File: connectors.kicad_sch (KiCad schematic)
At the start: 15 parts, among them J1 Compute-Module-4_Plug_Connect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, Q3 DZDH0401DW, Q9 AO3401A, U20 NTS0102_XSON, U21 NTS0102_XSON

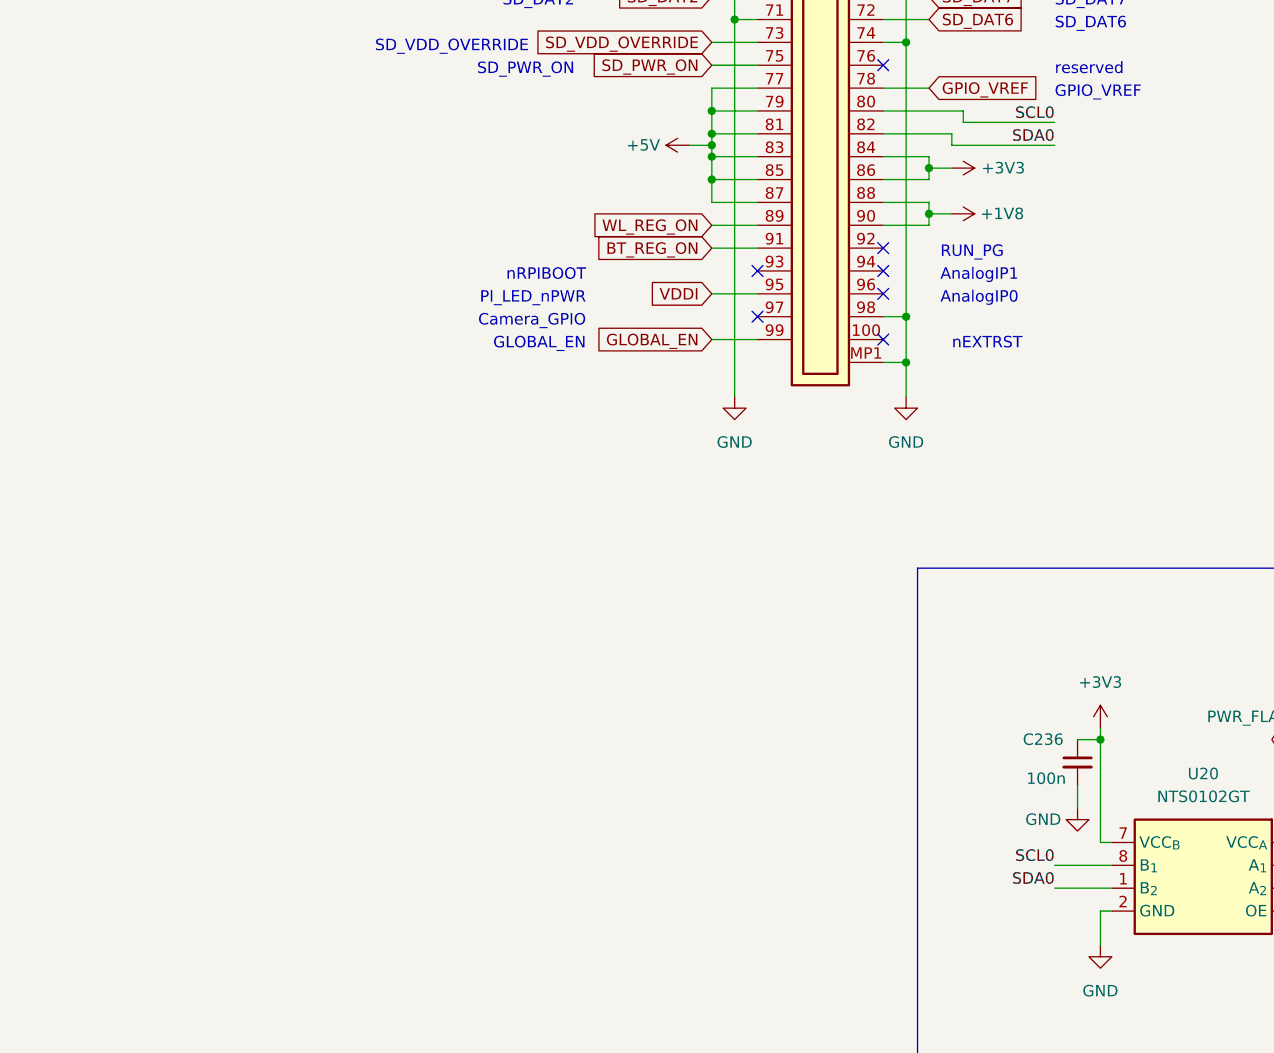
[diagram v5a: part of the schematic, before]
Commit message: [#57422] Update PI_LED_nPWR pin connection
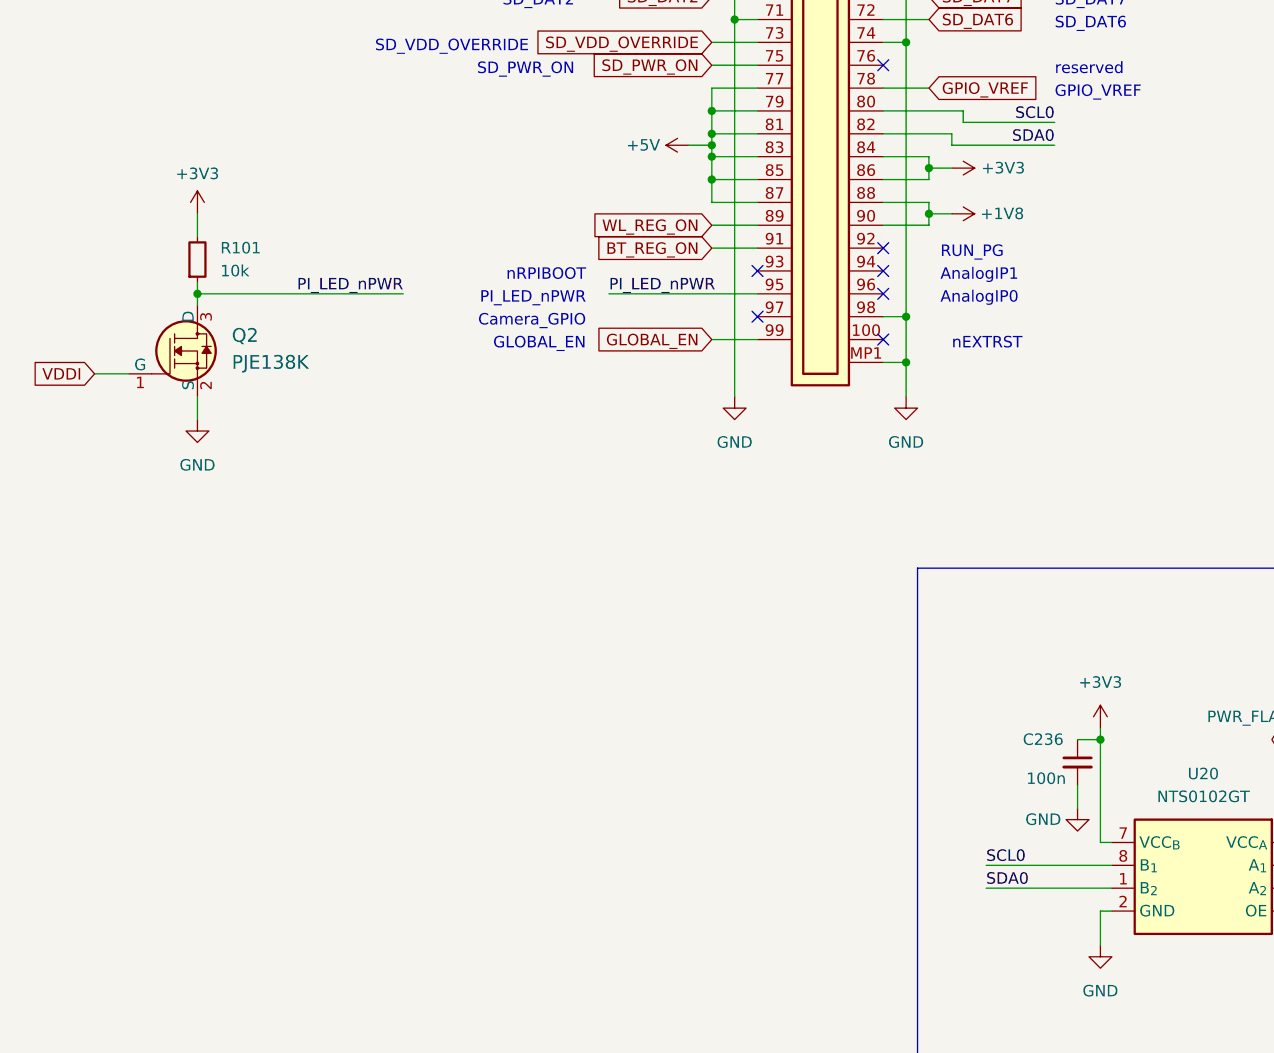
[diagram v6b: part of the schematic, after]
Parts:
- added Q2: PJE138K, antmicro-footprints:SOT-523, symbol antmicroTransistorsFETsMOSFETsSingle:PJE138K
- added R101: R_10k_0402, antmicro-footprints:R_0402_1005Metric, symbol antmicroResistors0402:R_10k_0402
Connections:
- net +3V3: now also R101.2
- net GND: now also Q2.2 (S)
- net VDDI: now also Q2.1 (G); no longer J1.95
- new net PI_LED_nPWR: J1.95, Q2.3 (D), R101.1

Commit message: [#57422] Update DNP
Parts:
- R15, R62: now not fitted
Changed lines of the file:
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@@
   )
   (symbol (lib_id "antmicroResistors0402:R_10k_0402") (at 170.18 140.97 180) (unit 1)
-    (in_bom yes) (on_board yes) (dnp no)
+    (in_bom yes) (on_board yes) (dnp yes)
     (property "Reference" "R15" (at 161.29 142.24 0)
       (effects (font (size 1.27 1.27) (thickness 0.15)) (justify right))
@@
     )
     (property "DNP" "DNP" (at 167.64 140.97 0)
-      (effects (font (size 1.27 1.27)))
+      (effects (font (size 1.27 1.27)) hide)
     )
     (pin "1")
@@
   )
   (symbol (lib_id "antmicroResistors0603:R_0R_22.4A_0603") (at 227.33 124.46 0) (unit 1)
-    (in_bom yes) (on_board yes) (dnp no)
+    (in_bom yes) (on_board yes) (dnp yes)
     (property "Reference" "R62" (at 229.87 119.38 0)
       (effects (font (size 1.27 1.27) (thickness 0.15)))
@@
     )
     (property "DNP" "DNP" (at 229.87 124.46 0)
-      (effects (font (size 1.27 1.27)))
+      (effects (font (size 1.27 1.27)) hide)
     )
     (pin "1")

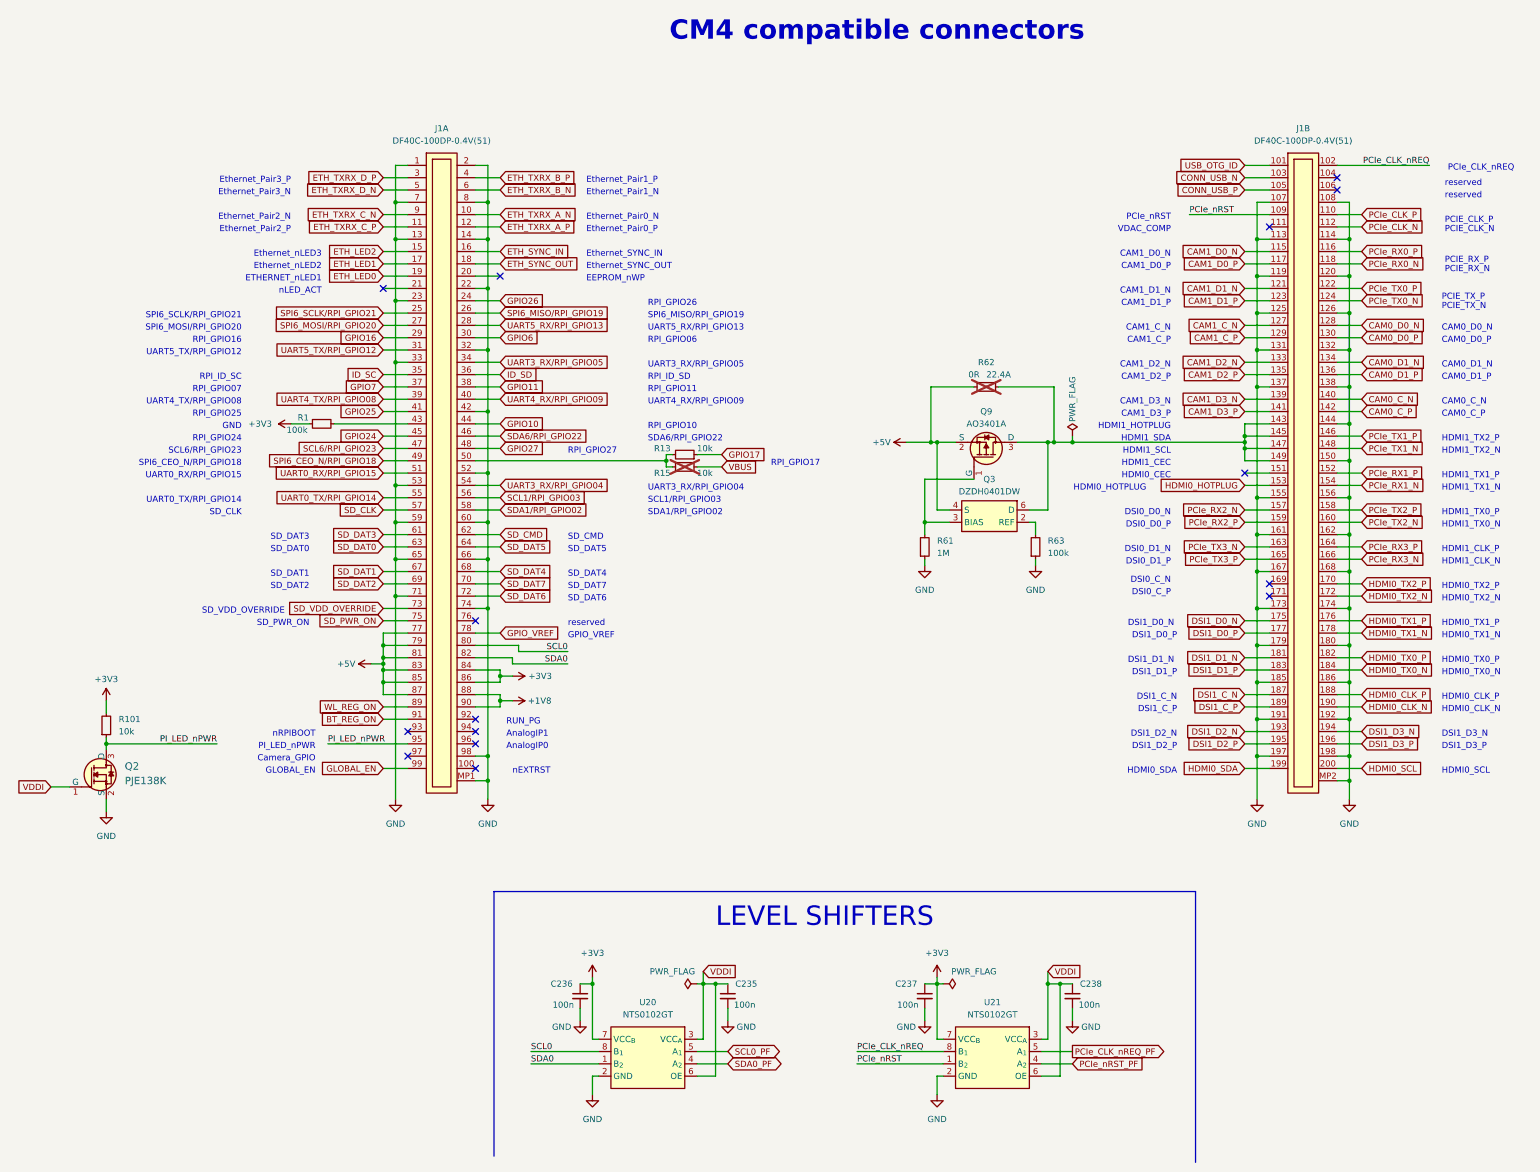
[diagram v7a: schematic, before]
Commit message: [#57505] Start reworking schematic to hierarchical structure
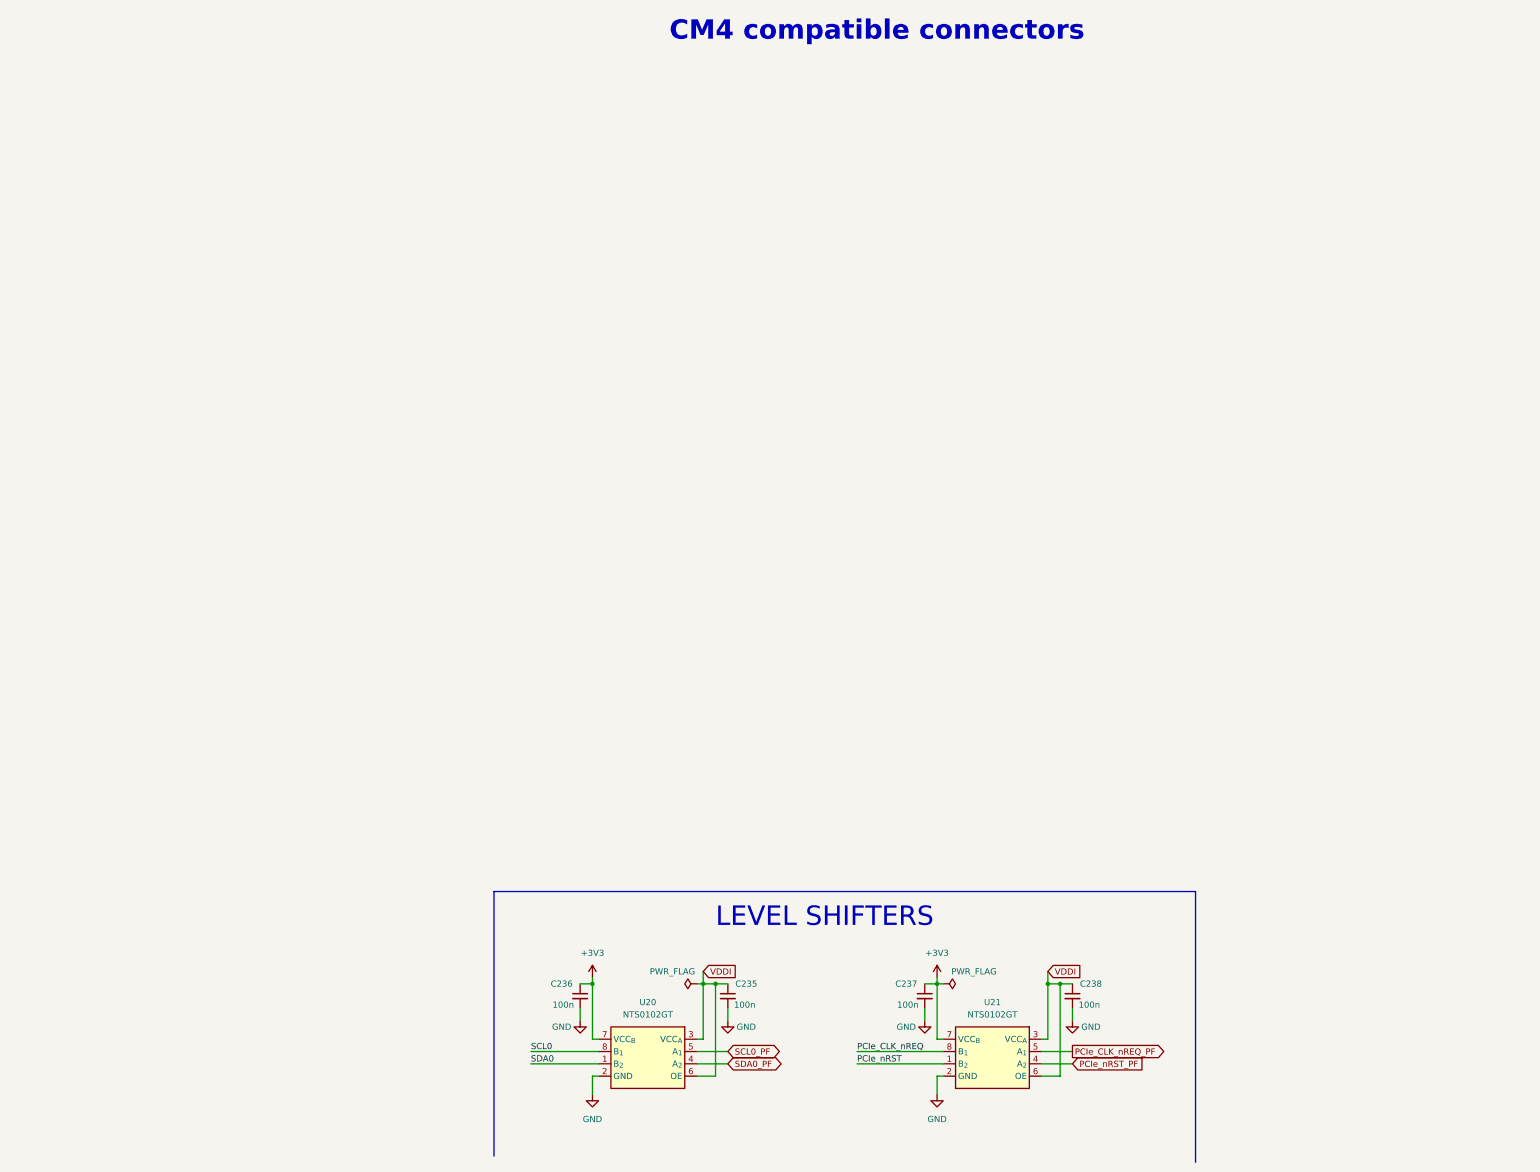
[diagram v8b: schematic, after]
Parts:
- removed J1: Compute-Module-4_Plug_Connector, antmicro-footprints:Compute-Module-4_Plug_Connector, symbol antmicroModules:Compute-Module-4_Plug_Connector
- removed Q2: PJE138K, antmicro-footprints:SOT-523, symbol antmicroTransistorsFETsMOSFETsSingle:PJE138K
- removed Q3: DZDH0401DW, antmicro-footprints:SOT-363, symbol antmicroPMICORControllersIdealDiodes:DZDH0401DW
- removed Q9: AO3401A, antmicro-footprints:SOT-23-3, symbol antmicroTransistorsFETsMOSFETsSingle:AO3401A
- removed R1, R63: R_100k_0402, antmicro-footprints:R_0402_1005Metric, symbol antmicroResistors0402:R_100k_0402
- removed R101, R13, R15: R_10k_0402, antmicro-footprints:R_0402_1005Metric, symbol antmicroResistors0402:R_10k_0402
- removed R61: R_1M_0402, antmicro-footprints:R_0402_1005Metric, symbol antmicroResistors0402:R_1M_0402
- removed R62: R_0R_22.4A_0603, antmicro-footprints:R_0603_1608Metric, symbol antmicroResistors0603:R_0R_22.4A_0603
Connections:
- no-connect marks 15 -> 0
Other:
- note removed: "AnalogIP0"
- note removed: "AnalogIP1"
- note removed: "CAM0_C_N"
- note removed: "CAM0_C_P"
- note removed: "CAM0_D0_N"
- note removed: "CAM0_D0_P"
- note removed: "CAM0_D1_N"
- note removed: "CAM0_D1_P"
- note removed: "CAM1_C_N"
- note removed: "CAM1_C_P"
- note removed: "CAM1_D0_N"
- note removed: "CAM1_D0_P"
- note removed: "CAM1_D1_N"
- note removed: "CAM1_D1_P"
- note removed: "CAM1_D2_N"
- note removed: "CAM1_D2_P"
- note removed: "CAM1_D3_N"
- note removed: "CAM1_D3_P"
- note removed: "Camera_GPIO"
- note removed: "DSI0_C_N"
- note removed: "DSI0_C_P"
- note removed: "DSI0_D0_N"
- note removed: "DSI0_D0_P"
- note removed: "DSI0_D1_N"
- note removed: "DSI0_D1_P"
- note removed: "DSI1_C_N"
- note removed: "DSI1_C_P"
- note removed: "DSI1_D0_N"
- note removed: "DSI1_D0_P"
- note removed: "DSI1_D1_N"
- note removed: "DSI1_D1_P"
- note removed: "DSI1_D2_N"
- note removed: "DSI1_D2_P"
- note removed: "DSI1_D3_N"
- note removed: "DSI1_D3_P"
- note removed: "EEPROM_nWP"
- note removed: "ETHERNET_nLED1"
- note removed: "Ethernet_Pair0_N"
- note removed: "Ethernet_Pair0_P"
- note removed: "Ethernet_Pair1_N"
- note removed: "Ethernet_Pair1_P"
- note removed: "Ethernet_Pair2_N"
- note removed: "Ethernet_Pair2_P"
- note removed: "Ethernet_Pair3_N"
- note removed: "Ethernet_Pair3_P"
- note removed: "Ethernet_SYNC_IN"
- note removed: "Ethernet_SYNC_OUT"
- note removed: "Ethernet_nLED2"
- note removed: "Ethernet_nLED3"
- note removed: "GLOBAL_EN"
- note removed: "GND"
- note removed: "GPIO_VREF"
- note removed: "HDMI0_CEC"
- note removed: "HDMI0_CLK_N"
- note removed: "HDMI0_CLK_P"
- note removed: "HDMI0_HOTPLUG"
- note removed: "HDMI0_SCL"
- note removed: "HDMI0_SDA"
- note removed: "HDMI0_TX0_N"
- note removed: "HDMI0_TX0_P"
- note removed: "HDMI0_TX1_N"
- note removed: "HDMI0_TX1_P"
- note removed: "HDMI0_TX2_N"
- note removed: "HDMI0_TX2_P"
- note removed: "HDMI1_CEC"
- note removed: "HDMI1_CLK_N"
- note removed: "HDMI1_CLK_P"
- note removed: "HDMI1_HOTPLUG"
- note removed: "HDMI1_SCL"
- note removed: "HDMI1_SDA"
- note removed: "HDMI1_TX0_N"
- note removed: "HDMI1_TX0_P"
- note removed: "HDMI1_TX1_N"
- note removed: "HDMI1_TX1_P"
- note removed: "HDMI1_TX2_N"
- note removed: "HDMI1_TX2_P"
- note removed: "PCIE_CLK_N"
- note removed: "PCIE_CLK_P"
- note removed: "PCIE_RX_N"
- note removed: "PCIE_RX_P"
- note removed: "PCIE_TX_N"
- note removed: "PCIE_TX_P"
- note removed: "PCIe_CLK_nREQ"
- note removed: "PCIe_nRST"
- note removed: "PI_LED_nPWR"
- note removed: "RPI_GPIO06"
- note removed: "RPI_GPIO07"
- note removed: "RPI_GPIO10"
- note removed: "RPI_GPIO11"
- note removed: "RPI_GPIO16"
- note removed: "RPI_GPIO17"
- note removed: "RPI_GPIO24"
- note removed: "RPI_GPIO25"
- note removed: "RPI_GPIO26"
- note removed: "RPI_GPIO27"
- note removed: "RPI_ID_SC"
- note removed: "RPI_ID_SD"
- note removed: "RUN_PG"
- note removed: "SCL1/RPI_GPIO03"
- note removed: "SCL6/RPI_GPIO23"
- note removed: "SDA1/RPI_GPIO02"
- note removed: "SDA6/RPI_GPIO22"
- note removed: "SD_CLK"
- note removed: "SD_CMD"
- note removed: "SD_DAT0"
- note removed: "SD_DAT1"
- note removed: "SD_DAT2"
- note removed: "SD_DAT3"
- note removed: "SD_DAT4"
- note removed: "SD_DAT5"
- note removed: "SD_DAT6"
- note removed: "SD_DAT7"
- note removed: "SD_PWR_ON"
- note removed: "SD_VDD_OVERRIDE"
- note removed: "SPI6_CEO_N/RPI_GPIO18"
- note removed: "SPI6_MISO/RPI_GPIO19"
- note removed: "SPI6_MOSI/RPI_GPIO20"
- note removed: "SPI6_SCLK/RPI_GPIO21"
- note removed: "UART0_RX/RPI_GPIO15"
- note removed: "UART0_TX/RPI_GPIO14"
- note removed: "UART3_RX/RPI_GPIO04"
- note removed: "UART3_RX/RPI_GPIO05"
- note removed: "UART4_RX/RPI_GPIO09"
- note removed: "UART4_TX/RPI_GPIO08"
- note removed: "UART5_RX/RPI_GPIO13"
- note removed: "UART5_TX/RPI_GPIO12"
- note removed: "VDAC_COMP"
- note removed: "nEXTRST"
- note removed: "nLED_ACT"
- note removed: "nRPIBOOT"
- note removed: "reserved"
